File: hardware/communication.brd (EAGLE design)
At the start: 33.5 x 34.6 mm, 44 parts, among them J1 MICRO_USB_B_HIROSE_ZX62-B-5PA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, SW1 TVAF06-A020B-R, U2 NJM12888F, X1 FA-238

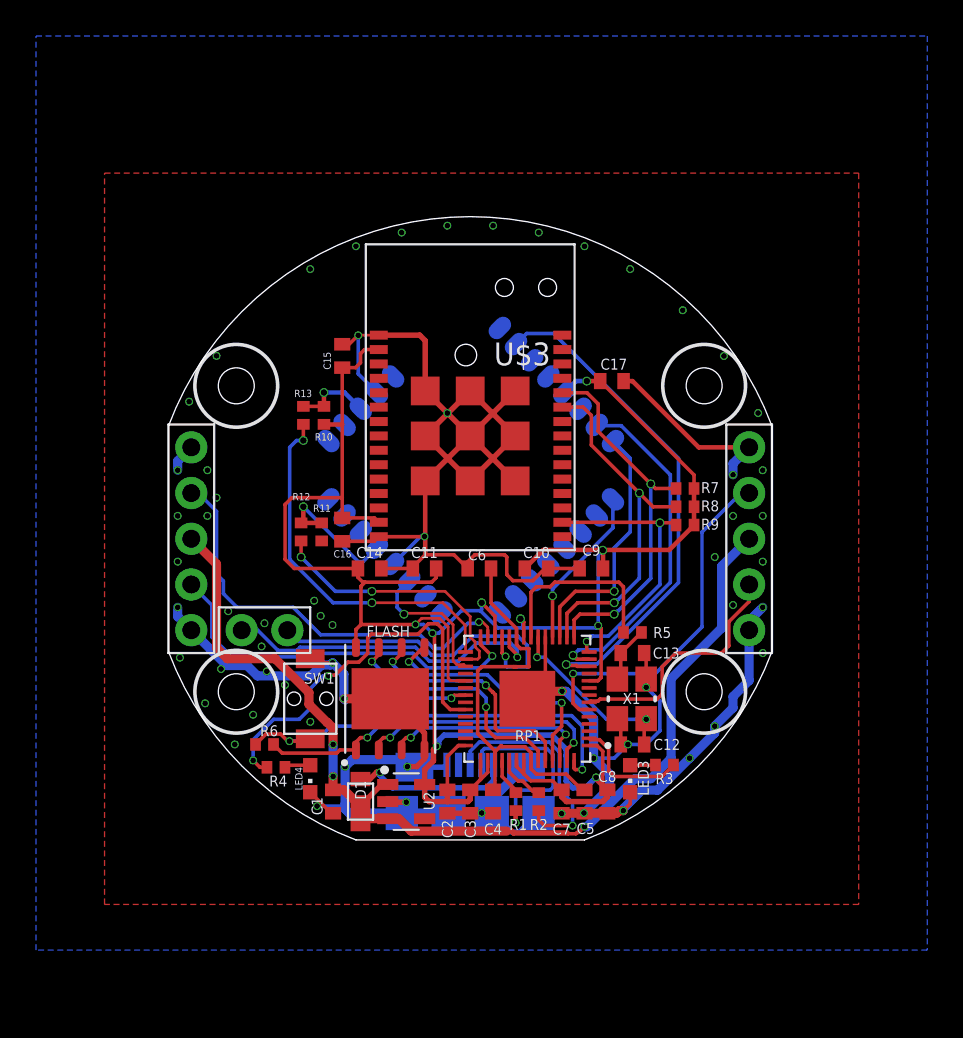
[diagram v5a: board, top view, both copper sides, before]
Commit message: LiPoのだけできなかったのですが、それ以外のべたGND済のものです。
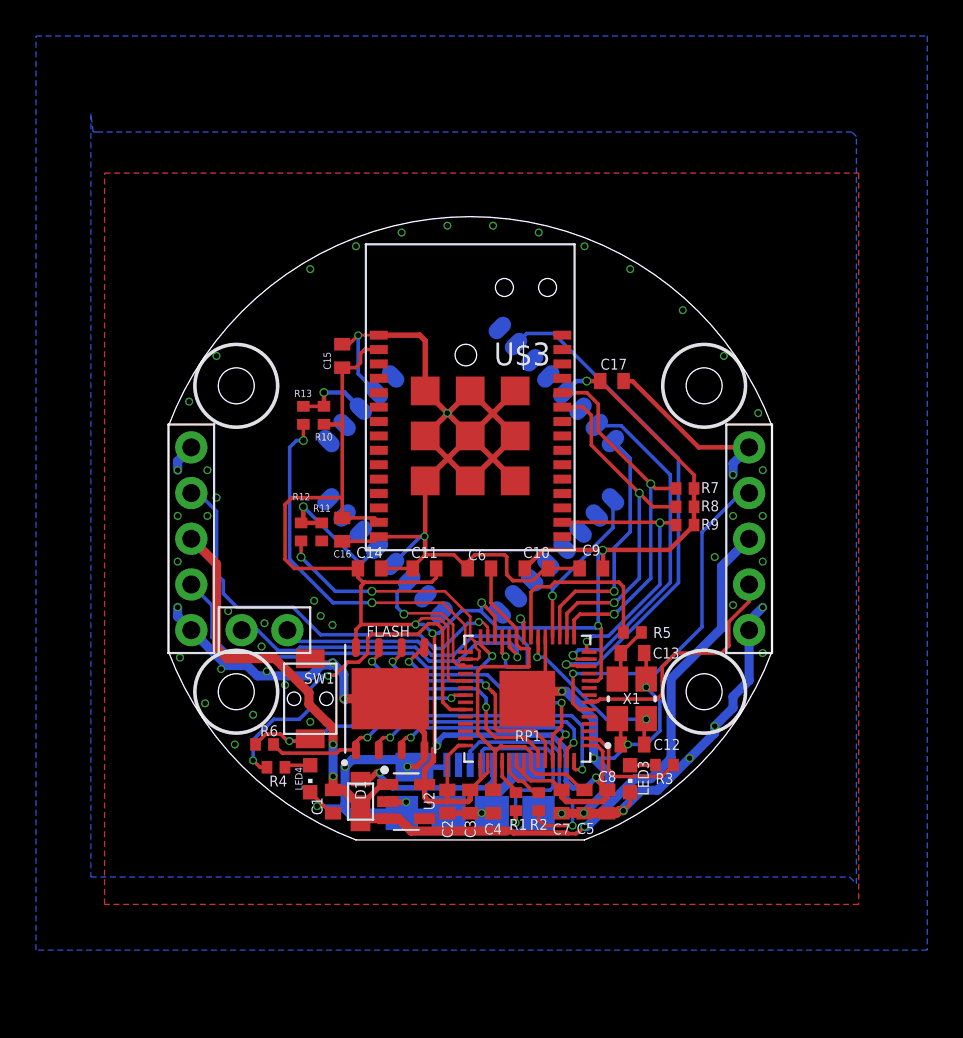
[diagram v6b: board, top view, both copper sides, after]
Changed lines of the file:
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@@
 <wire x1="-8.376" y1="-14.726" x2="-8.376" y2="-14.599" width="0.2" layer="1"/>
 <wire x1="-1.27" y1="-15.255" x2="0" y2="-15.255" width="0.3048" layer="1"/>
-<wire x1="11.811" y1="12.7" x2="14.097" y2="10.16" width="0" layer="19" extent="1-1"/>
-<wire x1="16.002" y1="6.985" x2="14.097" y2="10.16" width="0" layer="19" extent="1-1"/>
-<wire x1="15.5" y1="5.08" x2="16.002" y2="6.985" width="0" layer="19" extent="1-1"/>
-<wire x1="16.256" y1="3.81" x2="15.5" y2="5.08" width="0" layer="19" extent="1-1"/>
-<wire x1="14.605" y1="1.27" x2="14.605" y2="3.556" width="0" layer="19" extent="1-1"/>
-<wire x1="16.256" y1="1.27" x2="14.605" y2="1.27" width="0" layer="19" extent="1-1"/>
-<wire x1="13.589" y1="-1.016" x2="14.605" y2="1.27" width="0" layer="19" extent="1-1"/>
-<wire x1="16.256" y1="-1.27" x2="16.256" y2="1.27" width="0" layer="19" extent="1-1"/>
-<wire x1="16.256" y1="-3.81" x2="16.256" y2="-1.27" width="0" layer="19" extent="1-1"/>
-<wire x1="6.3165" y1="-15.241" x2="6.35" y2="-15.255" width="0" layer="19" extent="1-1"/>
-<wire x1="-1.27" y1="-15.255" x2="-1.2" y2="-15.24" width="0" layer="19" extent="1-16"/>
-<wire x1="-3.49" y1="-12.6605" x2="-3.1" y2="-12.69" width="0" layer="19" extent="16-16"/>
-<wire x1="0.635" y1="-15.24" x2="1.2" y2="-15.24" width="0" layer="19" extent="16-16"/>
-<wire x1="16.256" y1="-6.35" x2="15.5" y2="-5.08" width="0" layer="19" extent="1-1"/>
-<wire x1="-16.129" y1="-6.604" x2="-15.5" y2="-5.08" width="0" layer="19" extent="1-1"/>
-<wire x1="14.605" y1="-3.683" x2="16.256" y2="-3.81" width="0" layer="19" extent="1-1"/>
-<wire x1="-10.287" y1="-8.128" x2="-8.89" y2="-6.665" width="0" layer="19" extent="1-1"/>
-<wire x1="-11.303" y1="-7.366" x2="-10.287" y2="-8.128" width="0" layer="19" extent="1-1"/>
-<wire x1="-11.592" y1="-5.985" x2="-11.303" y2="-7.366" width="0" layer="19" extent="1-1"/>
-<wire x1="-11.4345" y1="-4.6935" x2="-11.592" y2="-5.985" width="0" layer="19" extent="1-1"/>
-<wire x1="-13.45" y1="-4.0235" x2="-11.4345" y2="-4.6935" width="0" layer="19" extent="1-1"/>
-<wire x1="-7.6525" y1="-4.7915" x2="-7.6455" y2="-6.8955" width="0" layer="19" extent="1-1"/>
-<wire x1="-8.31" y1="-4.287" x2="-7.6525" y2="-4.7915" width="0" layer="19" extent="1-1"/>
-<wire x1="-8.673" y1="-3.442" x2="-8.31" y2="-4.287" width="0" layer="19" extent="1-1"/>
-<wire x1="-8.886" y1="-10.1735" x2="-7.0195" y2="-8.89" width="0" layer="19" extent="1-1"/>
-<wire x1="-13.843" y1="-7.239" x2="-16.129" y2="-6.604" width="0" layer="19" extent="1-1"/>
-<wire x1="-14.732" y1="-9.144" x2="-13.843" y2="-7.239" width="0" layer="19" extent="1-1"/>
-<wire x1="-12.065" y1="-9.779" x2="-10.287" y2="-8.128" width="0" layer="19" extent="1-1"/>
-<wire x1="-13.081" y1="-11.43" x2="-12.065" y2="-9.779" width="0" layer="19" extent="1-1"/>
-<wire x1="-16.256" y1="-1.27" x2="-16.256" y2="-3.81" width="0" layer="19" extent="1-1"/>
-<wire x1="-16.256" y1="1.27" x2="-16.256" y2="-1.27" width="0" layer="19" extent="1-1"/>
-<wire x1="-14.605" y1="1.27" x2="-16.256" y2="1.27" width="0" layer="19" extent="1-1"/>
-<wire x1="-14.097" y1="2.286" x2="-14.605" y2="1.27" width="0" layer="19" extent="1-1"/>
-<wire x1="-14.605" y1="3.81" x2="-14.097" y2="2.286" width="0" layer="19" extent="1-1"/>
-<wire x1="-15.5" y1="5.08" x2="-14.605" y2="3.81" width="0" layer="19" extent="1-1"/>
-<wire x1="-15.621" y1="7.62" x2="-15.5" y2="5.08" width="0" layer="19" extent="1-1"/>
-<wire x1="-14.097" y1="10.16" x2="-15.621" y2="7.62" width="0" layer="19" extent="1-1"/>
-<wire x1="-8.255" y1="-0.119" x2="-8.673" y2="-3.442" width="0" layer="19" extent="1-1"/>
-<wire x1="-7.112" y1="-0.142" x2="-8.255" y2="-0.119" width="0" layer="19" extent="1-1"/>
-<wire x1="-4.28563125" y1="-1.401375" x2="-4.938" y2="-1.651" width="0" layer="19" extent="1-16"/>
-<wire x1="-2.5" y1="5.715" x2="-2.5" y2="3.215" width="0" layer="19" extent="1-1"/>
-<wire x1="-1.27" y1="6.985" x2="-2.5" y2="5.715" width="0" layer="19" extent="1-1"/>
-<wire x1="-2.5" y1="8.215" x2="-1.27" y2="6.985" width="0" layer="19" extent="1-1"/>
-<wire x1="-6.223" y1="11.303" x2="-7.112" y2="10.81" width="0" layer="19" extent="1-1"/>
-<wire x1="0" y1="5.715" x2="-1.27" y2="6.985" width="0" layer="19" extent="1-1"/>
-<wire x1="8.89" y1="14.986" x2="11.811" y2="12.7" width="0" layer="19" extent="1-1"/>
-<wire x1="6.35" y1="16.256" x2="8.89" y2="14.986" width="0" layer="19" extent="1-1"/>
-<wire x1="3.81" y1="17.018" x2="6.35" y2="16.256" width="0" layer="19" extent="1-1"/>
-<wire x1="1.27" y1="17.399" x2="3.81" y2="17.018" width="0" layer="19" extent="1-1"/>
-<wire x1="-1.27" y1="17.399" x2="1.27" y2="17.399" width="0" layer="19" extent="1-1"/>
-<wire x1="-3.81" y1="17.018" x2="-1.27" y2="17.399" width="0" layer="19" extent="1-1"/>
-<wire x1="-6.35" y1="16.256" x2="-3.81" y2="17.018" width="0" layer="19" extent="1-1"/>
-<wire x1="-8.89" y1="14.986" x2="-6.35" y2="16.256" width="0" layer="19" extent="1-1"/>
+<polygon width="0.1524" layer="16">
+<vertex x="-21.082" y="23.622"/>
+<vertex x="-21.082" y="-18.796"/>
+<vertex x="21.082" y="-18.796"/>
+<vertex x="21.463" y="-19.177"/>
+<vertex x="21.463" y="22.352"/>
+<vertex x="21.209" y="22.606"/>
+<vertex x="-20.701" y="22.606"/>
+<vertex x="-20.955" y="22.606"/>
+</polygon>
 </signal>
 <signal name="USB_DM">

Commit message: LoRa ResetとTWELITE TX&RXの引き出しピンを追加
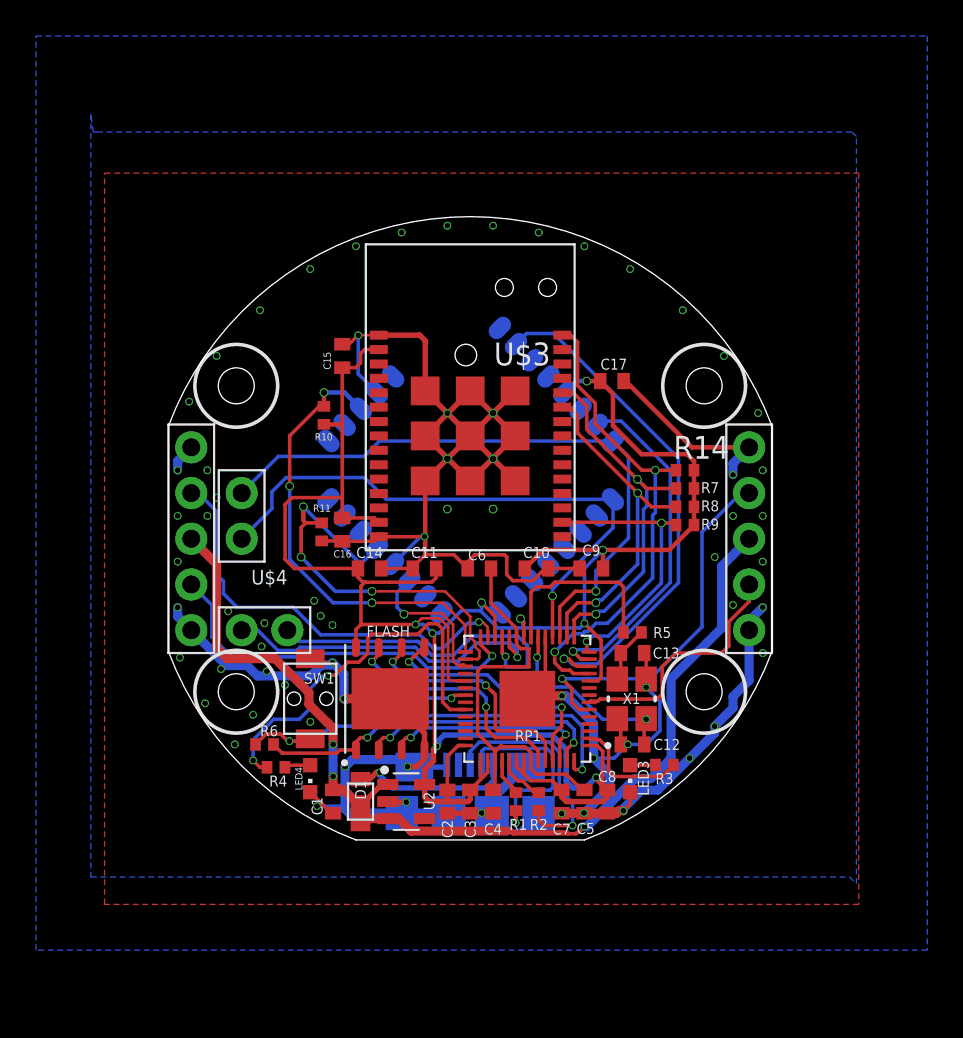
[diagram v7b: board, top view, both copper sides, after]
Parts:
- removed R12, R13: 1k, rcl:R0402
- added R14: 10k, rcl:R0402
- added U$4: P2_2_2.54, pins:P2_2.54
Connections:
- new net ROLA_!RESET!: R14.1, RP1.11, U$3.P30
- net TWE_RESET: no longer R12.1, R12.2
- net TWE_RTX: now also U$4.P$2
- net TWE_SLEEP: no longer R13.1, R13.2
- net TWE_TRX: now also U$4.P$1
- net VDD: now also R14.2
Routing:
- net ROLA_!RESET!: track 0.00 -> 27.5 mm, vias 0 -> 2
- net TWE_TRX: track 9.04 -> 32.1 mm
- net TWE_RTX: track 14.2 -> 35.3 mm
- net VDD: track 134.3 -> 135.7 mm
- net ROLA_RTX: track 20.5 -> 19.5 mm
- net TWE_RESET: track 22.7 -> 23.6 mm
- net GND: track 177.4 -> 178.1 mm, vias 62 -> 68
- net XIN1: track 10.2 -> 10.9 mm
- net TX1: track 19.7 -> 20.4 mm

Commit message: シルクを調整
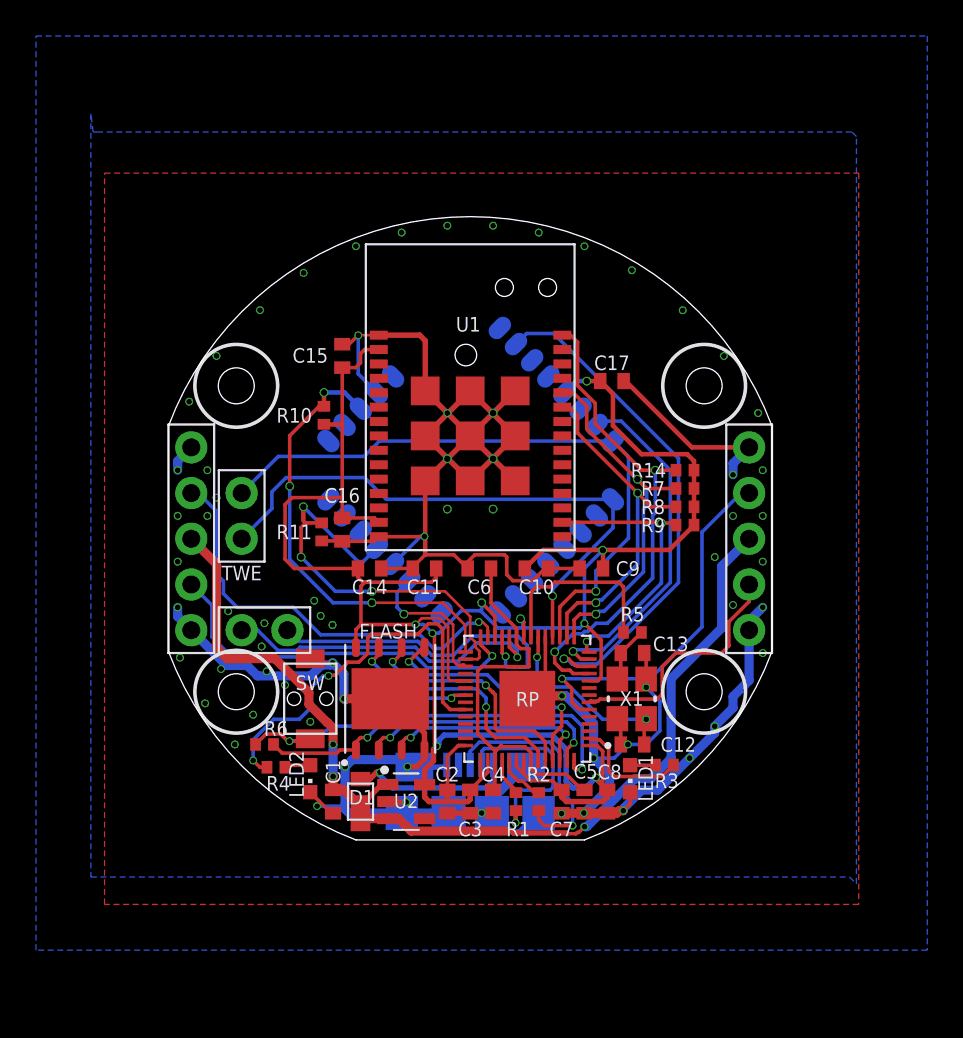
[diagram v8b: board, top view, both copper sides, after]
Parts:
- renumbered LED3 to LED1, LED4 to LED2, RP1 to RP, SW1 to SW, U$3 to U1, U$4 to TWE
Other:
- board text added: "TERES Comm Module"
- board text removed: "TERES Module"
